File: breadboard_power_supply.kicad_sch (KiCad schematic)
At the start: 17 parts, among them J1 PJ-059AH, J11 Conn_01x12_Male, J13 Conn_01x04_Male, J4 Screw_Terminal_01x06, J6 Conn_01x03_Male, J7 Screw_Terminal_01x02, U1 LM7805_TO220, U2 LM317_TO-220

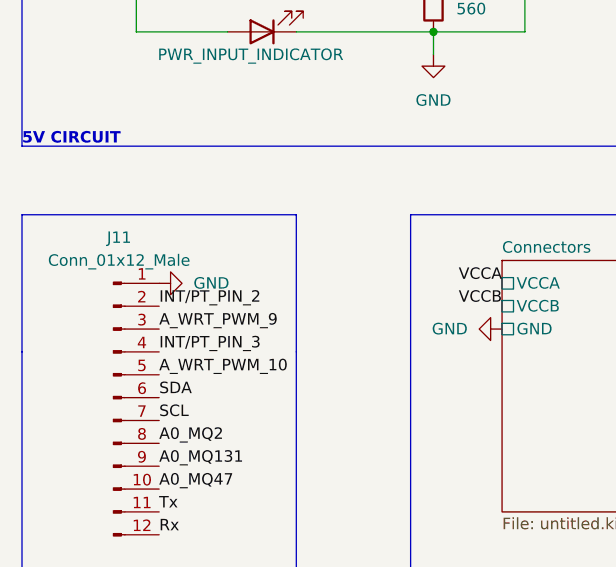
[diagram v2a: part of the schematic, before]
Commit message: Remaining : route tracking
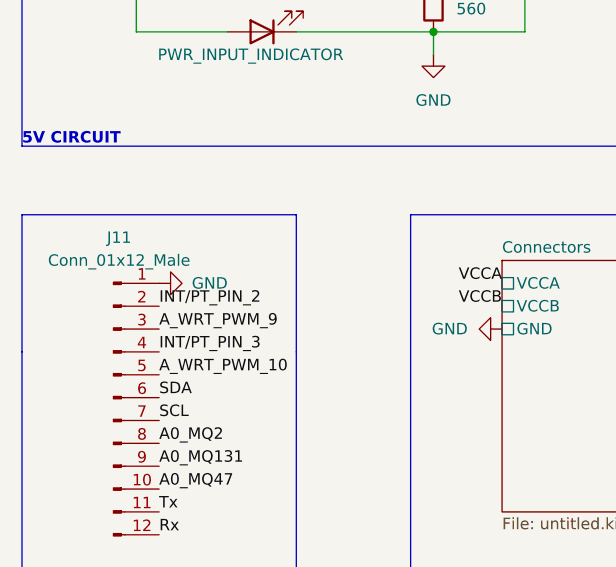
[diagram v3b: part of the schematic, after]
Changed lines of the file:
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@@
     (pin "2")
-  )
-  (symbol (lib_id "power:GND") (at 73.66 144.78 90) (unit 1)
-    (in_bom yes) (on_board yes) (fields_autoplaced)
-    (property "Reference" "#PWR0109" (id 0) (at 80.01 144.78 0)
-      (effects (font (size 1.27 1.27)) hide)
-    )
-    (property "Value" "GND" (id 1) (at 77.47 144.7799 90)
-      (effects (font (size 1.27 1.27)) (justify right))
-    )
-    (property "Footprint" "" (id 2) (at 73.66 144.78 0)
-      (effects (font (size 1.27 1.27)) hide)
-    )
-    (property "Datasheet" "" (id 3) (at 73.66 144.78 0)
-      (effects (font (size 1.27 1.27)) hide)
-    )
-    (pin "1")
   )
   (symbol (lib_id "Device:R") (at 104.14 100.33 180) (unit 1)
@@
     (pin "1")
   )
-  (symbol (lib_id "power:GND") (at 198.12 53.34 270) (unit 1)
-    (in_bom yes) (on_board yes) (fields_autoplaced)
-    (property "Reference" "#PWR0107" (id 0) (at 191.77 53.34 0)
-      (effects (font (size 1.27 1.27)) hide)
-    )
-    (property "Value" "GND" (id 1) (at 194.31 53.3399 90)
-      (effects (font (size 1.27 1.27)) (justify right))
-    )
-    (property "Footprint" "" (id 2) (at 198.12 53.34 0)
-      (effects (font (size 1.27 1.27)) hide)
-    )
-    (property "Datasheet" "" (id 3) (at 198.12 53.34 0)
-      (effects (font (size 1.27 1.27)) hide)
-    )
-    (pin "1")
-  )
   (symbol (lib_id "Device:C") (at 104.14 49.53 0) (unit 1)
     (in_bom yes) (on_board yes) (fields_autoplaced)
@@
     (pin "2")
   )
+  (symbol (lib_id "power:GND") (at 73.66 144.78 90) (unit 1)
+    (in_bom yes) (on_board yes)
+    (property "Reference" "#PWR0107" (id 0) (at 80.01 144.78 0)
+      (effects (font (size 1.27 1.27)) hide)
+    )
+    (property "Value" "GND" (id 1) (at 81.28 144.78 90)
+      (effects (font (size 1.27 1.27)) (justify left))
+    )
+    (property "Footprint" "" (id 2) (at 73.66 144.78 0)
+      (effects (font (size 1.27 1.27)) hide)
+    )
+    (property "Datasheet" "" (id 3) (at 73.66 144.78 0)
+      (effects (font (size 1.27 1.27)) hide)
+    )
+    (pin "1")
+  )
   (symbol (lib_id "power:PWR_FLAG") (at 73.66 91.44 0) (unit 1)
     (in_bom yes) (on_board yes) (fields_autoplaced)
@@
     (pin "3")
     (pin "4")
+  )
+  (symbol (lib_id "power:GND") (at 198.12 58.42 270) (unit 1)
+    (in_bom yes) (on_board yes) (fields_autoplaced)
+    (property "Reference" "#PWR0109" (id 0) (at 191.77 58.42 0)
+      (effects (font (size 1.27 1.27)) hide)
+    )
+    (property "Value" "GND" (id 1) (at 194.31 58.4199 90)
+      (effects (font (size 1.27 1.27)) (justify right))
+    )
+    (property "Footprint" "" (id 2) (at 198.12 58.42 0)
+      (effects (font (size 1.27 1.27)) hide)
+    )
+    (property "Datasheet" "" (id 3) (at 198.12 58.42 0)
+      (effects (font (size 1.27 1.27)) hide)
+    )
+    (pin "1")
+  )
+  (symbol (lib_id "power:GND") (at 198.12 53.34 270) (unit 1)
+    (in_bom yes) (on_board yes) (fields_autoplaced)
+    (property "Reference" "#PWR0108" (id 0) (at 191.77 53.34 0)
+      (effects (font (size 1.27 1.27)) hide)
+    )
+    (property "Value" "GND" (id 1) (at 194.31 53.3399 90)
+      (effects (font (size 1.27 1.27)) (justify right))
+    )
+    (property "Footprint" "" (id 2) (at 198.12 53.34 0)
+      (effects (font (size 1.27 1.27)) hide)
+    )
+    (property "Datasheet" "" (id 3) (at 198.12 53.34 0)
+      (effects (font (size 1.27 1.27)) hide)
+    )
+    (pin "1")
   )
   (symbol (lib_id "PJ-059AH:PJ-059AH") (at 66.04 50.8 0) (unit 1)
@@
     (pin "2")
     (pin "3")
-  )
-  (symbol (lib_id "power:GND") (at 198.12 58.42 270) (unit 1)
-    (in_bom yes) (on_board yes) (fields_autoplaced)
-    (property "Reference" "#PWR0108" (id 0) (at 191.77 58.42 0)
-      (effects (font (size 1.27 1.27)) hide)
-    )
-    (property "Value" "GND" (id 1) (at 194.31 58.4199 90)
-      (effects (font (size 1.27 1.27)) (justify right))
-    )
-    (property "Footprint" "" (id 2) (at 198.12 58.42 0)
-      (effects (font (size 1.27 1.27)) hide)
-    )
-    (property "Datasheet" "" (id 3) (at 198.12 58.42 0)
-      (effects (font (size 1.27 1.27)) hide)
-    )
-    (pin "1")
   )
   (symbol (lib_id "Connector:Conn_01x12_Male") (at 68.58 157.48 0) (unit 1)
@@
       (reference "#PWR0106") (unit 1) (value "GND") (footprint "")
     )
-    (path "/39226ee4-478e-43d6-b517-dff589b69f53"
+    (path "/49c5333a-44cb-4217-bda3-067bd76bc5b0"
       (reference "#PWR0107") (unit 1) (value "GND") (footprint "")
     )
-    (path "/c1ec35dc-7966-41f1-bee8-588d1fca77a6"
+    (path "/869167f9-8eb6-4517-9ac2-b8c44def3f41"
       (reference "#PWR0108") (unit 1) (value "GND") (footprint "")
     )
-    (path "/0ed54a9f-cef2-4aad-aa09-bf9da4b2b979"
+    (path "/84d70bf1-5884-42c3-8d73-99d2bbead97a"
       (reference "#PWR0109") (unit 1) (value "GND") (footprint "")
     )

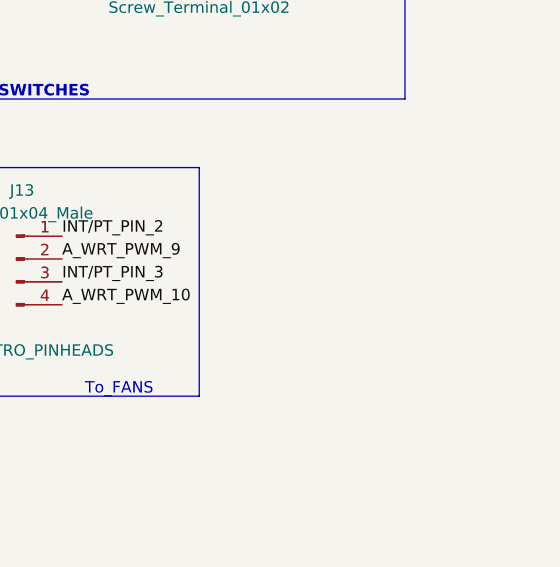
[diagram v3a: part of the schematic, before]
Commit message: Routing and Copper - hatch fills
proceeding
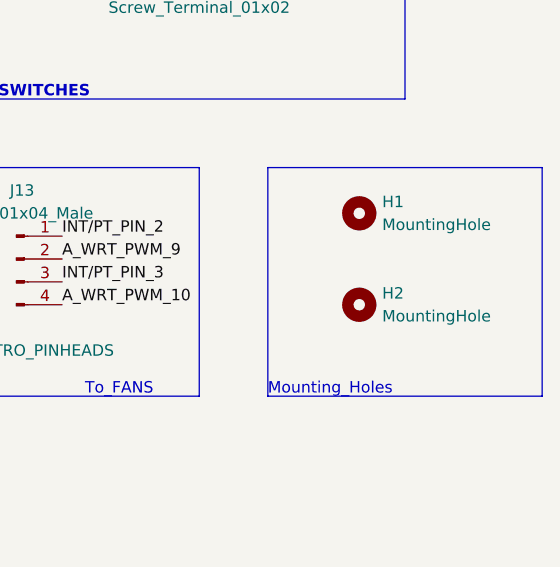
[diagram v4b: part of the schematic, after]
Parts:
- added H1, H2: MountingHole, MountingHole:MountingHole_2.7mm, symbol Mechanical:MountingHole
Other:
- note added: "Mounting_Holes"
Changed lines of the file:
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@@
   (junction (at 104.14 45.72) (diameter 0) (color 0 0 0 0)
   )
+  (polyline (pts (xy 248.92 162.56) (xy 248.92 137.16))
+    (stroke (width 0) (type default) (color 0 0 0 0))
+  )
   (wire (pts (xy 76.2 50.8) (xy 76.2 53.34))
     (stroke (width 0) (type default) (color 0 0 0 0))
@@
     (stroke (width 0) (type default) (color 0 0 0 0))
   )
+  (polyline (pts (xy 218.44 137.16) (xy 218.44 162.56))
+    (stroke (width 0) (type default) (color 0 0 0 0))
+  )
   (polyline (pts (xy 177.8 83.82) (xy 233.68 83.82))
     (stroke (width 0) (type default) (color 0 0 0 0))
@@
     (stroke (width 0) (type default) (color 0 0 0 0))
   )
+  (polyline (pts (xy 218.44 137.16) (xy 248.92 137.16))
+    (stroke (width 0) (type default) (color 0 0 0 0))
+  )
   (wire (pts (xy 88.9 116.84) (xy 104.14 116.84))
     (stroke (width 0) (type default) (color 0 0 0 0))
@@
   )
   (polyline (pts (xy 101.6 137.16) (xy 101.6 177.8))
+    (stroke (width 0) (type default) (color 0 0 0 0))
+  )
+  (polyline (pts (xy 218.44 162.56) (xy 248.92 162.56))
     (stroke (width 0) (type default) (color 0 0 0 0))
   )
@@
   )
   (text "Το_FANS" (at 198.12 162.56 0)
+    (effects (font (size 1.27 1.27)) (justify left bottom))
+  )
+  (text "Mounting_Holes" (at 218.44 162.56 0)
     (effects (font (size 1.27 1.27)) (justify left bottom))
   )
@@
     (pin "2")
   )
+  (symbol (lib_id "Mechanical:MountingHole") (at 228.6 152.4 0) (unit 1)
+    (in_bom yes) (on_board yes) (fields_autoplaced)
+    (property "Reference" "H2" (id 0) (at 231.14 151.1299 0)
+      (effects (font (size 1.27 1.27)) (justify left))
+    )
+    (property "Value" "MountingHole" (id 1) (at 231.14 153.6699 0)
+      (effects (font (size 1.27 1.27)) (justify left))
+    )
+    (property "Footprint" "MountingHole:MountingHole_2.7mm" (id 2) (at 228.6 152.4 0)
+      (effects (font (size 1.27 1.27)) hide)
+    )
+    (property "Datasheet" "~" (id 3) (at 228.6 152.4 0)
+      (effects (font (size 1.27 1.27)) hide)
+    )
+  )
   (symbol (lib_id "power:GND") (at 203.2 111.76 270) (unit 1)
     (in_bom yes) (on_board yes)
@@
     )
     (pin "1")
+  )
+  (symbol (lib_id "Mechanical:MountingHole") (at 228.6 142.24 0) (unit 1)
+    (in_bom yes) (on_board yes) (fields_autoplaced)
+    (property "Reference" "H1" (id 0) (at 231.14 140.9699 0)
+      (effects (font (size 1.27 1.27)) (justify left))
+    )
+    (property "Value" "MountingHole" (id 1) (at 231.14 143.5099 0)
+      (effects (font (size 1.27 1.27)) (justify left))
+    )
+    (property "Footprint" "MountingHole:MountingHole_2.7mm" (id 2) (at 228.6 142.24 0)
+      (effects (font (size 1.27 1.27)) hide)
+    )
+    (property "Datasheet" "~" (id 3) (at 228.6 142.24 0)
+      (effects (font (size 1.27 1.27)) hide)
+    )
   )
   (symbol (lib_id "Connector:Conn_01x03_Male") (at 208.28 96.52 180) (unit 1)
@@
       (reference "D1") (unit 1) (value "LED") (footprint "LED_SMD:LED_0805_2012Metric")
     )
+    (path "/9ceeff0a-ae63-43da-8fd2-e3d57063537d"
+      (reference "H1") (unit 1) (value "MountingHole") (footprint "MountingHole:MountingHole_2.7mm")
+    )
+    (path "/5d2f3ae9-e953-4b8b-8ec2-7e1e969f3fae"
+      (reference "H2") (unit 1) (value "MountingHole") (footprint "MountingHole:MountingHole_2.7mm")
+    )
     (path "/8ab99e8f-2f82-48ee-8bf9-bf07876cf96c"

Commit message: Redesign of the PCB
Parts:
- C1, C2, C3: footprint Capacitor_SMD:C_0805_2012Metric -> Capacitor_THT:C_Disc_D3.0mm_W2.0mm_P2.50mm
- D1: footprint LED_SMD:LED_0805_2012Metric -> LED_THT:LED_D5.0mm
- R1, R2, R3, R4, R5: footprint Resistor_SMD:R_0805_2012Metric -> Resistor_THT:R_Axial_DIN0204_L3.6mm_D1.6mm_P7.62mm_Horizontal
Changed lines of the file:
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@@
     (property "Reference" "D1" (id 0) (at 86.6775 109.22 0))
     (property "Value" "LED" (id 1) (at 86.6775 111.76 0))
-    (property "Footprint" "LED_SMD:LED_0805_2012Metric" (id 2) (at 85.09 116.84 0)
+    (property "Footprint" "LED_THT:LED_D5.0mm" (id 2) (at 85.09 116.84 0)
       (effects (font (size 1.27 1.27)) hide)
     )
@@
       (effects (font (size 1.27 1.27)) (justify right))
     )
-    (property "Footprint" "Resistor_SMD:R_0805_2012Metric" (id 2) (at 105.918 100.33 90)
+    (property "Footprint" "Resistor_THT:R_Axial_DIN0204_L3.6mm_D1.6mm_P7.62mm_Horizontal" (id 2) (at 105.918 100.33 90)
       (effects (font (size 1.27 1.27)) hide)
     )
@@
       (effects (font (size 1.27 1.27)) (justify left))
     )
-    (property "Footprint" "Capacitor_SMD:C_0805_2012Metric" (id 2) (at 105.1052 53.34 0)
+    (property "Footprint" "Capacitor_THT:C_Disc_D3.0mm_W2.0mm_P2.50mm" (id 2) (at 105.1052 53.34 0)
       (effects (font (size 1.27 1.27)) hide)
     )
@@
     (property "Reference" "R5" (id 0) (at 161.29 165.1 90))
     (property "Value" "1K" (id 1) (at 156.21 165.1 90))
-    (property "Footprint" "Resistor_SMD:R_0805_2012Metric" (id 2) (at 158.75 160.782 90)
+    (property "Footprint" "Resistor_THT:R_Axial_DIN0204_L3.6mm_D1.6mm_P7.62mm_Horizontal" (id 2) (at 158.75 160.782 90)
       (effects (font (size 1.27 1.27)) hide)
     )
@@
       (effects (font (size 1.27 1.27)) (justify left))
     )
-    (property "Footprint" "Capacitor_SMD:C_0805_2012Metric" (id 2) (at 115.2652 104.14 0)
+    (property "Footprint" "Capacitor_THT:C_Disc_D3.0mm_W2.0mm_P2.50mm" (id 2) (at 115.2652 104.14 0)
       (effects (font (size 1.27 1.27)) hide)
     )
@@
       (effects (font (size 1.27 1.27)) (justify right))
     )
-    (property "Footprint" "Resistor_SMD:R_0805_2012Metric" (id 2) (at 72.898 102.87 90)
+    (property "Footprint" "Resistor_THT:R_Axial_DIN0204_L3.6mm_D1.6mm_P7.62mm_Horizontal" (id 2) (at 72.898 102.87 90)
       (effects (font (size 1.27 1.27)) hide)
     )
@@
     (property "Reference" "R4" (id 0) (at 147.32 170.18 90))
     (property "Value" "2K" (id 1) (at 147.32 165.1 90))
-    (property "Footprint" "Resistor_SMD:R_0805_2012Metric" (id 2) (at 151.638 167.64 90)
+    (property "Footprint" "Resistor_THT:R_Axial_DIN0204_L3.6mm_D1.6mm_P7.62mm_Horizontal" (id 2) (at 151.638 167.64 90)
       (effects (font (size 1.27 1.27)) hide)
     )
@@
       (effects (font (size 1.27 1.27)) (justify left))
     )
-    (property "Footprint" "Capacitor_SMD:C_0805_2012Metric" (id 2) (at 140.6652 53.34 0)
+    (property "Footprint" "Capacitor_THT:C_Disc_D3.0mm_W2.0mm_P2.50mm" (id 2) (at 140.6652 53.34 0)
       (effects (font (size 1.27 1.27)) hide)
     )
@@
       (effects (font (size 1.27 1.27)) (justify right))
     )
-    (property "Footprint" "Resistor_SMD:R_0805_2012Metric" (id 2) (at 105.918 113.03 90)
+    (property "Footprint" "Resistor_THT:R_Axial_DIN0204_L3.6mm_D1.6mm_P7.62mm_Horizontal" (id 2) (at 105.918 113.03 90)
       (effects (font (size 1.27 1.27)) hide)
     )
@@
     )
     (path "/466ef885-12bc-4564-b8f6-796484be711c"
-      (reference "C1") (unit 1) (value "10u") (footprint "Capacitor_SMD:C_0805_2012Metric")
+      (reference "C1") (unit 1) (value "10u") (footprint "Capacitor_THT:C_Disc_D3.0mm_W2.0mm_P2.50mm")
     )
     (path "/e5617538-8520-4e0a-95ec-47eb41ed16dd"
-      (reference "C2") (unit 1) (value "0.1u") (footprint "Capacitor_SMD:C_0805_2012Metric")
+      (reference "C2") (unit 1) (value "0.1u") (footprint "Capacitor_THT:C_Disc_D3.0mm_W2.0mm_P2.50mm")
     )
     (path "/5adcc529-5723-4cd5-ab40-31266024c46e"
-      (reference "C3") (unit 1) (value "1u") (footprint "Capacitor_SMD:C_0805_2012Metric")
+      (reference "C3") (unit 1) (value "1u") (footprint "Capacitor_THT:C_Disc_D3.0mm_W2.0mm_P2.50mm")
     )
     (path "/0e292d95-89dc-49e8-83e0-8c7f031cfccc"
-      (reference "D1") (unit 1) (value "LED") (footprint "LED_SMD:LED_0805_2012Metric")
+      (reference "D1") (unit 1) (value "LED") (footprint "LED_THT:LED_D5.0mm")
     )
     (path "/9ceeff0a-ae63-43da-8fd2-e3d57063537d"
@@
     )
     (path "/186e5d8a-6772-4375-829b-19a2df6700c3"
-      (reference "R1") (unit 1) (value "180") (footprint "Resistor_SMD:R_0805_2012Metric")
+      (reference "R1") (unit 1) (value "180") (footprint "Resistor_THT:R_Axial_DIN0204_L3.6mm_D1.6mm_P7.62mm_Horizontal")
     )
     (path "/6fe50946-2be9-4286-9b3d-a1ad70deb934"
-      (reference "R2") (unit 1) (value "330") (footprint "Resistor_SMD:R_0805_2012Metric")
+      (reference "R2") (unit 1) (value "330") (footprint "Resistor_THT:R_Axial_DIN0204_L3.6mm_D1.6mm_P7.62mm_Horizontal")
     )
     (path "/e6b45546-c8d6-458a-90b9-8ea17a804c93"
-      (reference "R3") (unit 1) (value "560") (footprint "Resistor_SMD:R_0805_2012Metric")
+      (reference "R3") (unit 1) (value "560") (footprint "Resistor_THT:R_Axial_DIN0204_L3.6mm_D1.6mm_P7.62mm_Horizontal")
     )
     (path "/7bbcded8-64a3-4e9e-9a6c-c6b328f2ab4f"
-      (reference "R4") (unit 1) (value "2K") (footprint "Resistor_SMD:R_0805_2012Metric")
+      (reference "R4") (unit 1) (value "2K") (footprint "Resistor_THT:R_Axial_DIN0204_L3.6mm_D1.6mm_P7.62mm_Horizontal")
     )
     (path "/46fe53bc-7e23-4e72-b64a-08723b42c8bd"
-      (reference "R5") (unit 1) (value "1K") (footprint "Resistor_SMD:R_0805_2012Metric")
+      (reference "R5") (unit 1) (value "1K") (footprint "Resistor_THT:R_Axial_DIN0204_L3.6mm_D1.6mm_P7.62mm_Horizontal")
     )
     (path "/2ddb316c-3eb5-4c4d-93f7-046968649e30"
